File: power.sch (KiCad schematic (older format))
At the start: 1 part, among them U4 SST25VF032B

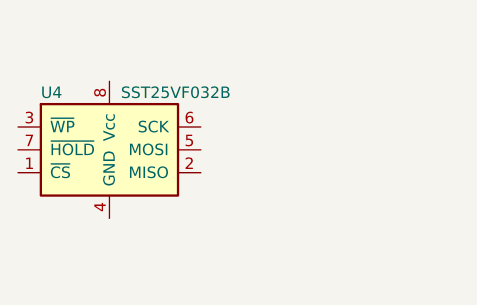
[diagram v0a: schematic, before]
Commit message: voltage regulators
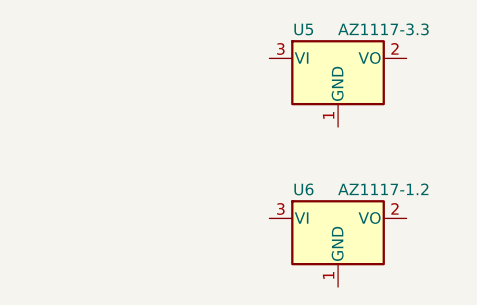
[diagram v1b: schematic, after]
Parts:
- removed U4: SST25VF032B, SOA008-150mil:SOA008-150mil, symbol MB85RS16
- added U5: AZ1117-3.3, TO_SOT_Packages_SMD:SOT-223, symbol AZ1117-3.3
- added U6: AZ1117-1.2, TO_SOT_Packages_SMD:SOT-223, symbol AZ1117-1.2
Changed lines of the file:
@@
 $Descr A4 11693 8268
 encoding utf-8
-Sheet 6 9
+Sheet 9 9
 Title ""
 Date ""
@@
 $EndDescr
 $Comp
-L MB85RS16 U4
-U 1 1 5A12E0C4
-P 2850 2600
-F 0 "U4" H 2550 2850 50  0000 L CNN
-F 1 "SST25VF032B" H 2900 2850 50  0000 L CNN
-F 2 "SOA008-150mil:SOA008-150mil" H 2500 2550 50  0001 C CNN
-F 3 "http://www.nxlab.fer.hr/dl/sst_flash.pdf" H 2500 2550 50  0001 C CNN
-	1    2850 2600
+L AZ1117-1.2 U6
+U 1 1 5A133D19
+P 3850 2900
+F 0 "U6" H 3700 3025 50  0000 C CNN
+F 1 "AZ1117-1.2" H 3850 3025 50  0000 L CNN
+F 2 "TO_SOT_Packages_SMD:SOT-223" H 3850 3150 50  0001 C CIN
+F 3 "" H 3850 2900 50  0001 C CNN
+	1    3850 2900
 	1    0    0    -1
 $EndComp
+$Comp
+L AZ1117-3.3 U5
+U 1 1 5A133D60
+P 3850 2200
+F 0 "U5" H 3700 2325 50  0000 C CNN
+F 1 "AZ1117-3.3" H 3850 2325 50  0000 L CNN
+F 2 "TO_SOT_Packages_SMD:SOT-223" H 3850 2450 50  0001 C CIN
+F 3 "" H 3850 2200 50  0001 C CNN
+	1    3850 2200
+	1    0    0    -1
+$EndComp
